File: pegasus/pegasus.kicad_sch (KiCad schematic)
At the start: 10 parts, among them IC1 RFD900, IC2 Adafruit_MPL3115A2, IC3 Adafruit-BNO055-PCB, IC4 L70B-M39, IC5 L7805ACV, J1 Conn_01x02_Female, J2 Conn_01x02_Female, U1 Teensy4.1, U2 CON-SMA-EDGE-S, U3 CON-SMA-EDGE-S

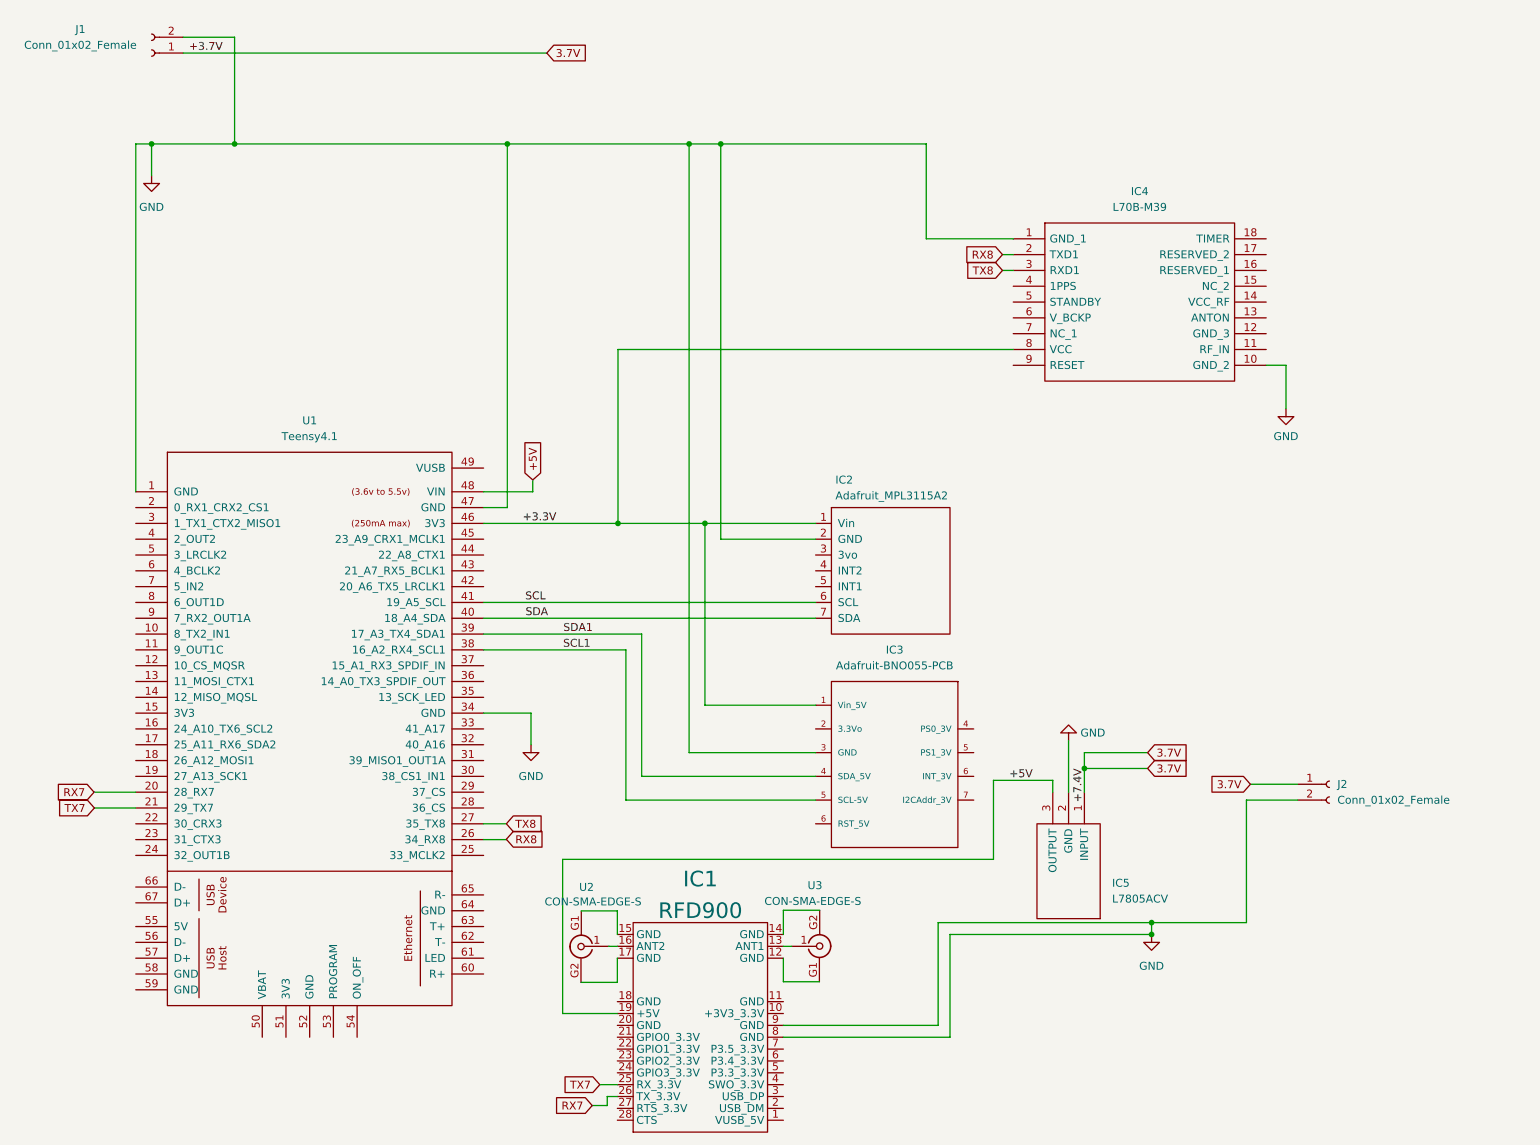
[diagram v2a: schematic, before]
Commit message: adjusted trace width for 5V power, added mounting holes, some 3D models
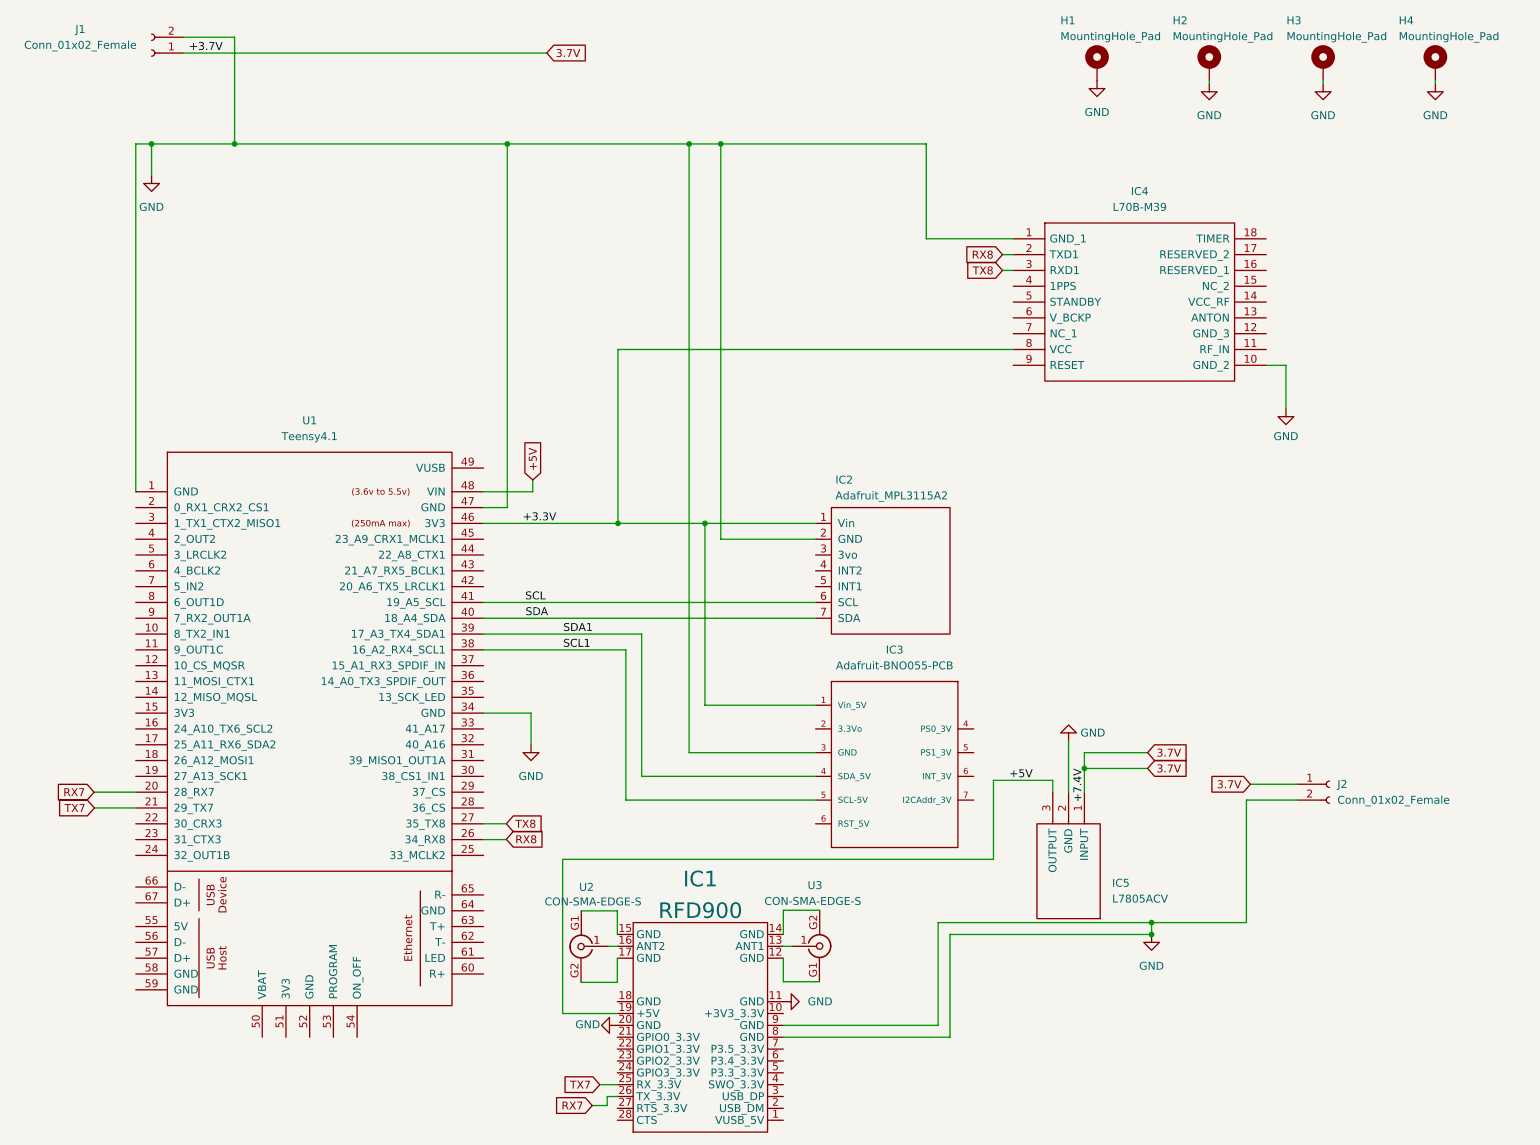
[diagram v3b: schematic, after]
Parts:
- added H1, H2, H3, H4: MountingHole_Pad, MountingHole:MountingHole_2.2mm_M2_Pad, symbol Mechanical:MountingHole_Pad
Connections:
- net GND: now also IC1.11 (GND), IC1.20 (GND), H1.1, H2.1, H3.1, H4.1
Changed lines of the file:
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@@
+    (stroke (width 0) (type default) (color 0 0 0 0))
+  )
+  (wire (pts (xy 214.376 25.908) (xy 214.376 25.4))
     (stroke (width 0) (type default) (color 0 0 0 0))
   )
@@
     (stroke (width 0) (type default) (color 0 0 0 0))
   )
+  (wire (pts (xy 250.698 25.908) (xy 250.698 25.4))
+    (stroke (width 0) (type default) (color 0 0 0 0))
+  )
   (wire (pts (xy 116.459 186.69) (xy 119.2784 186.69))
     (stroke (width 0) (type default) (color 0 0 0 0))
@@
   )
   (wire (pts (xy 44.45 35.56) (xy 57.785 35.56))
+    (stroke (width 0) (type default) (color 0 0 0 0))
+  )
+  (wire (pts (xy 232.664 25.4) (xy 232.664 25.908))
     (stroke (width 0) (type default) (color 0 0 0 0))
   )
@@
     (pin "1")
   )
+  (symbol (lib_id "power:GND") (at 145.9484 173.355 90) (unit 1)
+    (in_bom yes) (on_board yes) (fields_autoplaced)
+    (property "Reference" "#PWR0102" (id 0) (at 152.2984 173.355 0)
+      (effects (font (size 1.27 1.27)) hide)
+    )
+    (property "Value" "GND" (id 1) (at 149.86 173.3549 90)
+      (effects (font (size 1.27 1.27)) (justify right))
+    )
+    (property "Footprint" "" (id 2) (at 145.9484 173.355 0)
+      (effects (font (size 1.27 1.27)) hide)
+    )
+    (property "Datasheet" "" (id 3) (at 145.9484 173.355 0)
+      (effects (font (size 1.27 1.27)) hide)
+    )
+    (pin "1")
+  )
   (symbol (lib_id "power:GND") (at 226.695 78.105 0) (unit 1)
     (in_bom yes) (on_board yes) (fields_autoplaced)
@@
     (pin "3")
   )
+  (symbol (lib_id "Mechanical:MountingHole_Pad") (at 250.698 22.86 0) (unit 1)
+    (in_bom yes) (on_board yes)
+    (property "Reference" "H4" (id 0) (at 244.8052 15.748 0)
+      (effects (font (size 1.27 1.27)) (justify left))
+    )
+    (property "Value" "MountingHole_Pad" (id 1) (at 244.8052 18.288 0)
+      (effects (font (size 1.27 1.27)) (justify left))
+    )
+    (property "Footprint" "MountingHole:MountingHole_2.2mm_M2_Pad" (id 2) (at 250.698 22.86 0)
+      (effects (font (size 1.27 1.27)) hide)
+    )
+    (property "Datasheet" "~" (id 3) (at 250.698 22.86 0)
+      (effects (font (size 1.27 1.27)) hide)
+    )
+    (pin "1")
+  )
+  (symbol (lib_id "power:GND") (at 196.342 25.4 0) (unit 1)
+    (in_bom yes) (on_board yes) (fields_autoplaced)
+    (property "Reference" "#PWR0103" (id 0) (at 196.342 31.75 0)
+      (effects (font (size 1.27 1.27)) hide)
+    )
+    (property "Value" "GND" (id 1) (at 196.342 30.48 0))
+    (property "Footprint" "" (id 2) (at 196.342 25.4 0)
+      (effects (font (size 1.27 1.27)) hide)
+    )
+    (property "Datasheet" "" (id 3) (at 196.342 25.4 0)
+      (effects (font (size 1.27 1.27)) hide)
+    )
+    (pin "1")
+  )
+  (symbol (lib_id "power:GND") (at 214.376 25.908 0) (unit 1)
+    (in_bom yes) (on_board yes) (fields_autoplaced)
+    (property "Reference" "#PWR0104" (id 0) (at 214.376 32.258 0)
+      (effects (font (size 1.27 1.27)) hide)
+    )
+    (property "Value" "GND" (id 1) (at 214.376 30.988 0))
+    (property "Footprint" "" (id 2) (at 214.376 25.908 0)
+      (effects (font (size 1.27 1.27)) hide)
+    )
+    (property "Datasheet" "" (id 3) (at 214.376 25.908 0)
+      (effects (font (size 1.27 1.27)) hide)
+    )
+    (pin "1")
+  )
+  (symbol (lib_id "power:GND") (at 119.2784 177.165 270) (unit 1)
+    (in_bom yes) (on_board yes)
+    (property "Reference" "#PWR0101" (id 0) (at 112.9284 177.165 0)
+      (effects (font (size 1.27 1.27)) hide)
+    )
+    (property "Value" "GND" (id 1) (at 112.522 177.038 90)
+      (effects (font (size 1.27 1.27)) (justify left))
+    )
+    (property "Footprint" "" (id 2) (at 119.2784 177.165 0)
+      (effects (font (size 1.27 1.27)) hide)
+    )
+    (property "Datasheet" "" (id 3) (at 119.2784 177.165 0)
+      (effects (font (size 1.27 1.27)) hide)
+    )
+    (pin "1")
+  )
   (symbol (lib_id "power:GND") (at 205.105 162.56 0) (unit 1)
     (in_bom yes) (on_board yes) (fields_autoplaced)
@@
     (pin "1")
   )
+  (symbol (lib_id "Mechanical:MountingHole_Pad") (at 214.376 22.86 0) (unit 1)
+    (in_bom yes) (on_board yes)
+    (property "Reference" "H2" (id 0) (at 208.4832 15.748 0)
+      (effects (font (size 1.27 1.27)) (justify left))
+    )
+    (property "Value" "MountingHole_Pad" (id 1) (at 208.4832 18.288 0)
+      (effects (font (size 1.27 1.27)) (justify left))
+    )
+    (property "Footprint" "MountingHole:MountingHole_2.2mm_M2_Pad" (id 2) (at 214.376 22.86 0)
+      (effects (font (size 1.27 1.27)) hide)
+    )
+    (property "Datasheet" "~" (id 3) (at 214.376 22.86 0)
+      (effects (font (size 1.27 1.27)) hide)
+    )
+    (pin "1")
+  )
+  (symbol (lib_id "power:GND") (at 250.698 25.908 0) (unit 1)
+    (in_bom yes) (on_board yes) (fields_autoplaced)
+    (property "Reference" "#PWR0106" (id 0) (at 250.698 32.258 0)
+      (effects (font (size 1.27 1.27)) hide)
+    )
+    (property "Value" "GND" (id 1) (at 250.698 30.988 0))
+    (property "Footprint" "" (id 2) (at 250.698 25.908 0)
+      (effects (font (size 1.27 1.27)) hide)
+    )
+    (property "Datasheet" "" (id 3) (at 250.698 25.908 0)
+      (effects (font (size 1.27 1.27)) hide)
+    )
+    (pin "1")
+  )
   (symbol (lib_id "power:GND") (at 44.45 40.64 0) (unit 1)
     (in_bom yes) (on_board yes) (fields_autoplaced)
@@
     )
     (property "Datasheet" "" (id 3) (at 44.45 40.64 0)
+      (effects (font (size 1.27 1.27)) hide)
+    )
+    (pin "1")
+  )
+  (symbol (lib_id "Mechanical:MountingHole_Pad") (at 232.664 22.86 0) (unit 1)
+    (in_bom yes) (on_board yes)
+    (property "Reference" "H3" (id 0) (at 226.7712 15.748 0)
+      (effects (font (size 1.27 1.27)) (justify left))
+    )
+    (property "Value" "MountingHole_Pad" (id 1) (at 226.7712 18.288 0)
+      (effects (font (size 1.27 1.27)) (justify left))
+    )
+    (property "Footprint" "MountingHole:MountingHole_2.2mm_M2_Pad" (id 2) (at 232.664 22.86 0)
+      (effects (font (size 1.27 1.27)) hide)
+    )
+    (property "Datasheet" "~" (id 3) (at 232.664 22.86 0)
       (effects (font (size 1.27 1.27)) hide)
     )
@@
     (pin "8")
     (pin "9")
+  )
+  (symbol (lib_id "power:GND") (at 232.664 25.908 0) (unit 1)
+    (in_bom yes) (on_board yes) (fields_autoplaced)
+    (property "Reference" "#PWR0105" (id 0) (at 232.664 32.258 0)
+      (effects (font (size 1.27 1.27)) hide)
+    )
+    (property "Value" "GND" (id 1) (at 232.664 30.988 0))
+    (property "Footprint" "" (id 2) (at 232.664 25.908 0)
+      (effects (font (size 1.27 1.27)) hide)
+    )
+    (property "Datasheet" "" (id 3) (at 232.664 25.908 0)
+      (effects (font (size 1.27 1.27)) hide)
+    )
+    (pin "1")
   )
   (symbol (lib_id "Adafruit_BNO055:Adafruit-BNO055-PCB") (at 164.465 140.335 180) (unit 1)
@@
     (pin "9")
   )
+  (symbol (lib_id "Mechanical:MountingHole_Pad") (at 196.342 22.86 0) (unit 1)
+    (in_bom yes) (on_board yes)
+    (property "Reference" "H1" (id 0) (at 190.4492 15.748 0)
+      (effects (font (size 1.27 1.27)) (justify left))
+    )
+    (property "Value" "MountingHole_Pad" (id 1) (at 190.4492 18.288 0)
+      (effects (font (size 1.27 1.27)) (justify left))
+    )
+    (property "Footprint" "MountingHole:MountingHole_2.2mm_M2_Pad" (id 2) (at 196.342 22.86 0)
+      (effects (font (size 1.27 1.27)) hide)
+    )
+    (property "Datasheet" "~" (id 3) (at 196.342 22.86 0)
+      (effects (font (size 1.27 1.27)) hide)
+    )
+    (pin "1")
+  )
   (symbol (lib_name "CON-SMA-EDGE-S_2") (lib_id "sma-connectors:CON-SMA-EDGE-S") (at 156.8704 164.5666 270) (unit 1)
     (in_bom yes) (on_board yes)
@@
       (reference "#PWR05") (unit 1) (value "GND") (footprint "")
     )
+    (path "/8aaafdc0-c91d-4b67-8cb4-c79ed5bae408"
+      (reference "#PWR0101") (unit 1) (value "GND") (footprint "")
+    )
+    (path "/3fa9edc2-9fbb-43b5-b42c-e2e44b077acf"
+      (reference "#PWR0102") (unit 1) (value "GND") (footprint "")
+    )
+    (path "/70e52f12-fb67-4276-ad30-28892fb20b86"
+      (reference "#PWR0103") (unit 1) (value "GND") (footprint "")
+    )
+    (path "/78a4a849-1c24-4beb-98bb-5d8b5b1babf4"
+      (reference "#PWR0104") (unit 1) (value "GND") (footprint "")
+    )
+    (path "/c629176b-abd3-4695-ae9b-e765a0bc8aed"
+      (reference "#PWR0105") (unit 1) (value "GND") (footprint "")
+    )
+    (path "/abaa90e7-ead3-4e66-bb3e-cc1d7a6daa0e"
+      (reference "#PWR0106") (unit 1) (value "GND") (footprint "")
+    )
+    (path "/fa097515-aa33-445e-a81c-63a2092f37d7"
+      (reference "H1") (unit 1) (value "MountingHole_Pad") (footprint "MountingHole:MountingHole_2.2mm_M2_Pad")
+    )
+    (path "/9b4a3d5d-bec5-404f-9d07-6bbf9e73bbb6"
+      (reference "H2") (unit 1) (value "MountingHole_Pad") (footprint "MountingHole:MountingHole_2.2mm_M2_Pad")
+    )
+    (path "/b9ff2bc9-2909-44de-b87f-01ae5ef3e5c6"
+      (reference "H3") (unit 1) (value "MountingHole_Pad") (footprint "MountingHole:MountingHole_2.2mm_M2_Pad")
+    )
+    (path "/6d52c2cd-3d4d-4e9f-8991-6c4289d279ca"
+      (reference "H4") (unit 1) (value "MountingHole_Pad") (footprint "MountingHole:MountingHole_2.2mm_M2_Pad")
+    )
     (path "/f48d253a-f718-462f-8e9d-c68bcb29b9ab"

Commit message: added no connection flag to schematics, fixed minor mistakes on PCB and in footprints
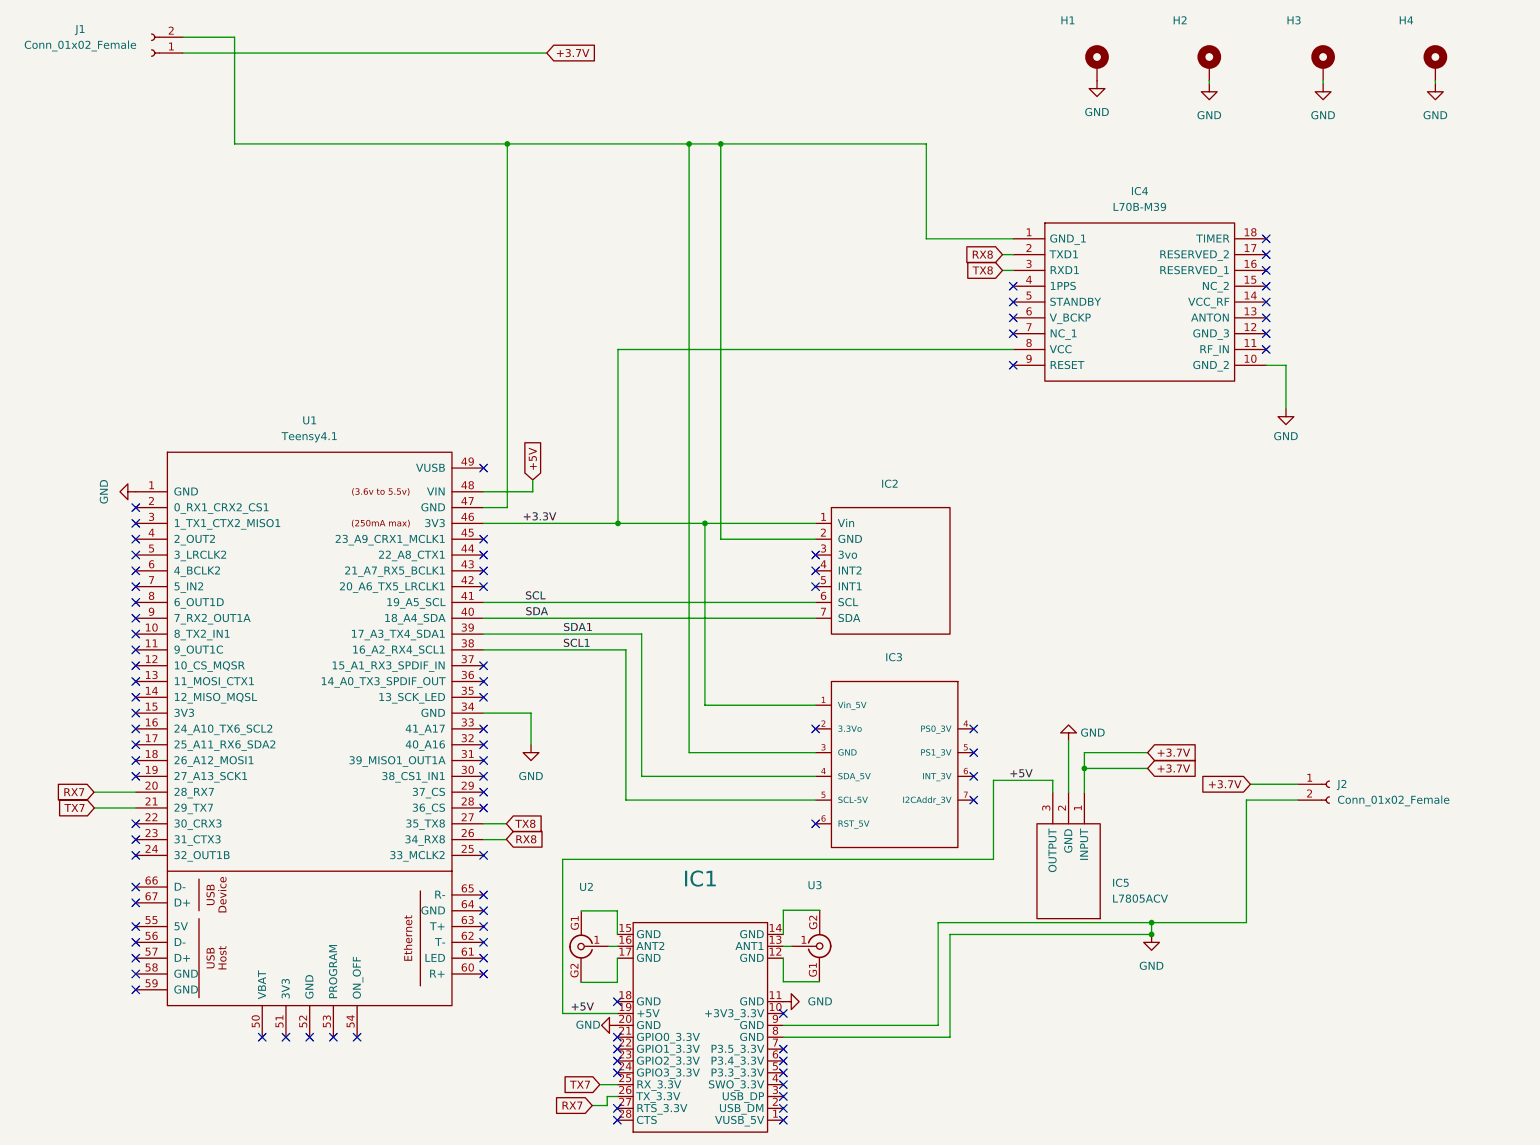
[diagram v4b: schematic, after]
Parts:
- H1, H2, H3, H4: value MountingHole_Pad -> (none); footprint MountingHole:MountingHole_2.2mm_M2_Pad -> (none); now left out of the parts list
- IC1: value RFD900 -> (none)
- IC2: value Adafruit_MPL3115A2 -> (none)
- IC3: value Adafruit-BNO055-PCB -> (none)
- U2, U3: value CON-SMA-EDGE-S -> (none); footprint SMA-Connectors:RFSOLUTIONS_CON-SMA-EDGE-S -> (none)
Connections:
- net GND: no longer IC2.2 (GND), IC3.3 (GND), IC4.1 (GND_1), J1.2 (Pin_2), U1.47 (GND)
- net 3.7V renamed +3.7V
- new net: IC2.2 (GND), IC3.3 (GND), IC4.1 (GND_1), J1.2 (Pin_2), U1.47 (GND)
- no-connect marks 0 -> 91
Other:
- moved on the sheet: IC2, IC3
